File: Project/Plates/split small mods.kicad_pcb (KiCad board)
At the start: 2 copper layers, 257.2 x 76.2 mm, 48 parts

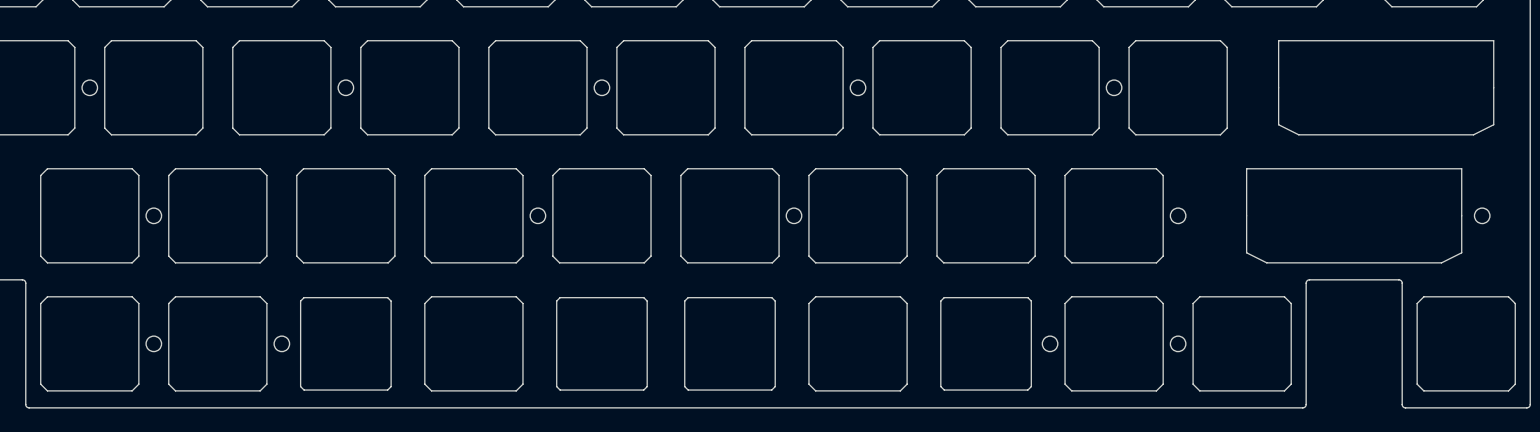
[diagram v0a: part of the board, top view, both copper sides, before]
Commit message: bottom row change, plate update, firmware update
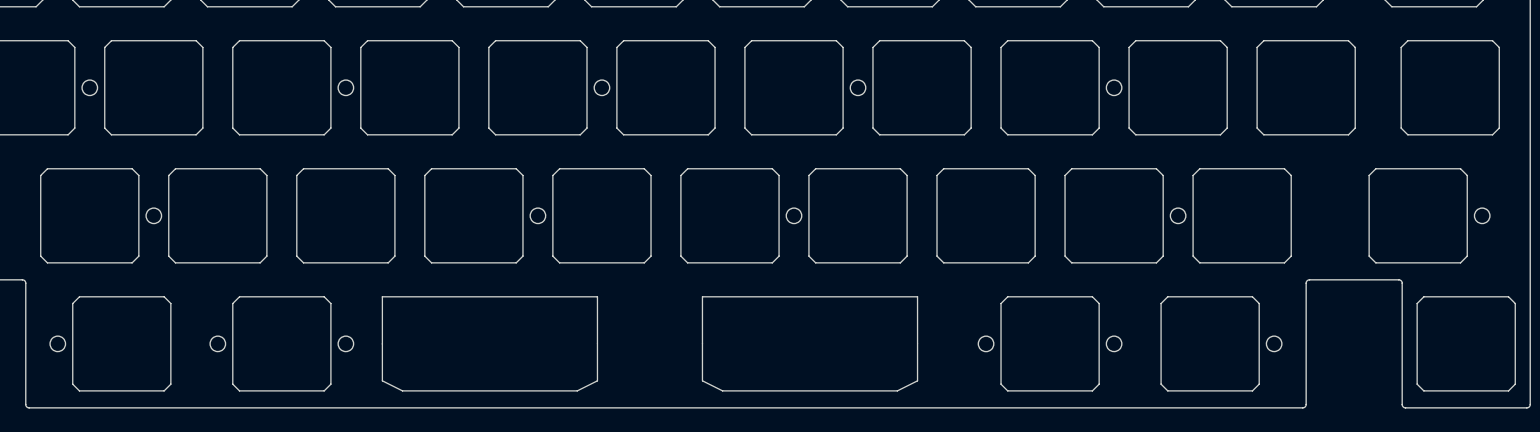
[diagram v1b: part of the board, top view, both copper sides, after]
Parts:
- removed the REF** at (174.6, 91.3) (x3)
- removed the REF** at (79.4, 91.3)
- removed the REF** at (117.5, 91.3) (x3)
- removed the REF** at (212.7, 91.3)
- removed the REF** at (248.4, 72.2)
- removed the REF** at (253.2, 53.2)
- removed the REF** at (60.3, 91.3)
- removed the REF** at (231.8, 91.3)
- added REF**: Value, cipulot_parts:ecs_plate_cut_1U, F.Cu at (203.2, 91.3)
- added REF**: Value, cipulot_parts:ecs_plate_cut_1U, F.Cu at (258.0, 72.2)
- added REF**: Value, cipulot_parts:ecs_plate_cut_1U, F.Cu at (262.7, 53.2)
- added REF**: Value, cipulot_parts:ecs_plate_cut_1U, F.Cu at (231.8, 72.2)
- added REF**: Value, cipulot_parts:ecs_plate_cut_2U, F.Cu at (167.5, 91.3)
- added REF**: Value, cipulot_parts:ecs_plate_cut_1U, F.Cu at (227.0, 91.3)
- added REF**: Value, cipulot_parts:ecs_plate_cut_1U, F.Cu at (65.1, 91.3)
- added REF**: Value, cipulot_parts:ecs_plate_cut_1U, F.Cu at (241.3, 53.2)
- added REF**: Value, cipulot_parts:ecs_plate_cut_2U, F.Cu at (119.9, 91.3)
- added REF**: Value, cipulot_parts:ecs_plate_cut_1U, F.Cu at (88.9, 91.3)
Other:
- outline, holes or cut-outs redrawn
